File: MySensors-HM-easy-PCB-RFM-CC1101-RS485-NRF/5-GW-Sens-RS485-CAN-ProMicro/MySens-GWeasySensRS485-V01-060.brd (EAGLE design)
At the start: 33 x 50 mm, 28 parts, among them IC1 LM1117MPX-ADJ, IC2 LD117ADT50TR, IC6 LM1117MPX-ADJ, X4 1751264

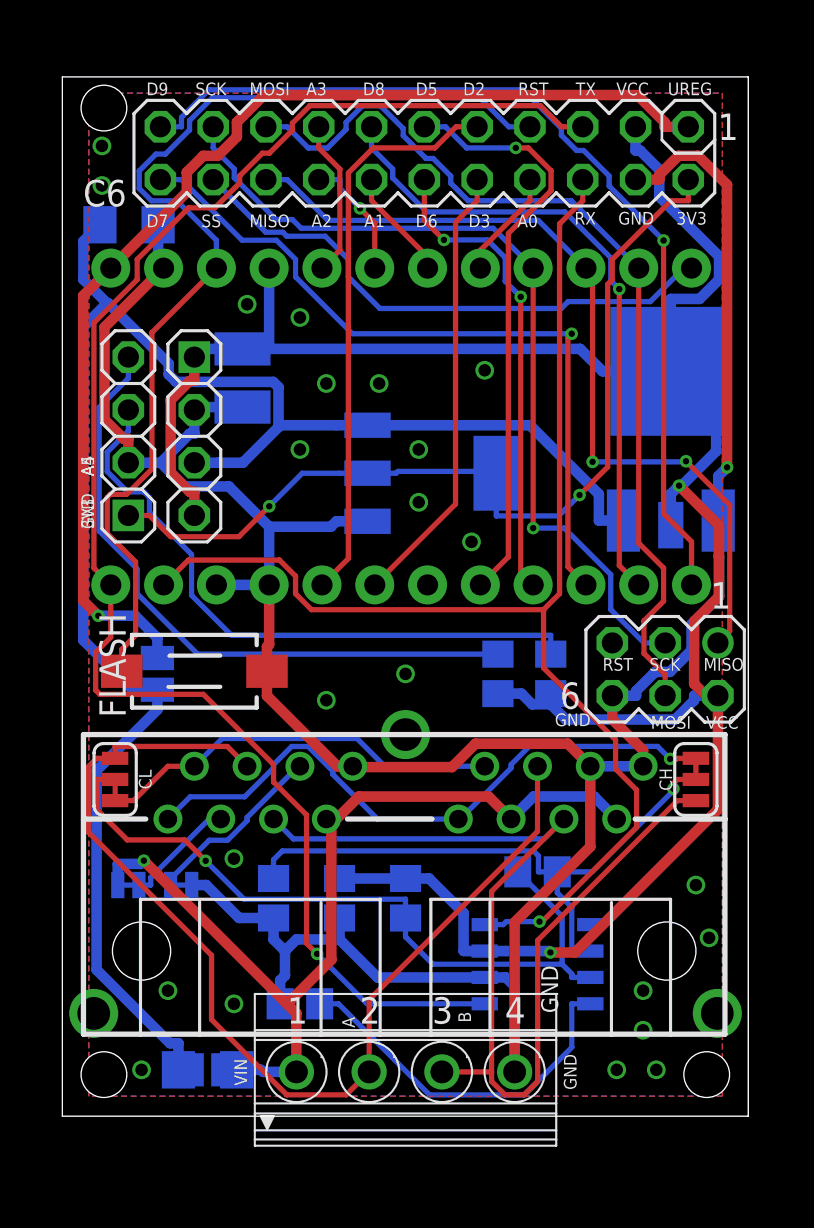
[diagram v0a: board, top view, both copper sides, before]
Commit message: CAN/RS485 Board
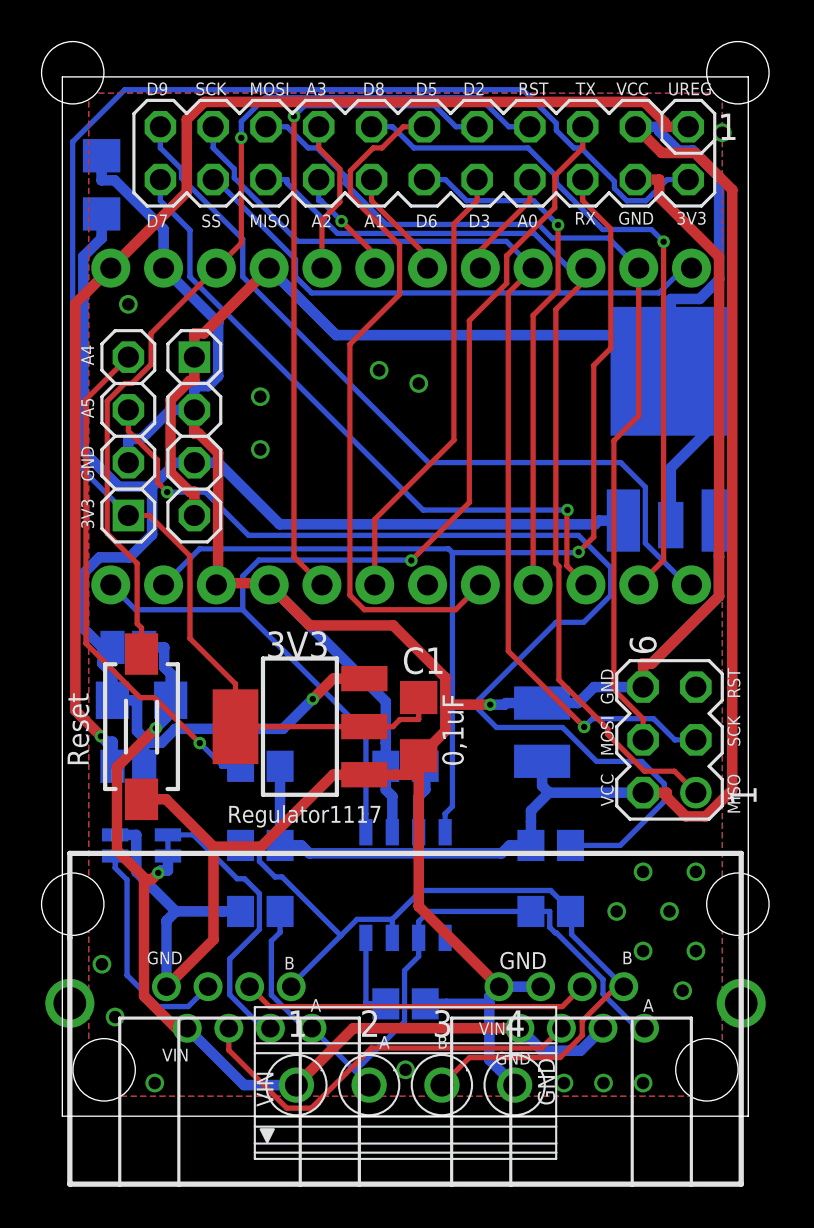
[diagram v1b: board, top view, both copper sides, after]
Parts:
- removed CH, CL: JUMPER-SMT_3_1-NC_TRACE_SILK, SparkFun-Jumpers:SMT-JUMPER_3_1-NC_TRACE_SILK
- added C1: 0.1uF, rcl:C1206
- J4: device RJ45:RJ45_2X_NARROW_SHILDPINS_NOCASE -> RJ45:RJ45_2X_S
- R3: value 680R -> 4K7
- R4: value 680R -> 4k7
- moved C4 22.3 mm to (23.1, 15.0), turned to 90 degrees
- moved RAW1 20.7 mm to (3.17, 19.1)
- moved F2 18.1 mm to (3.81, 16.5)
- moved IC1 13.7 mm to (11.4, 15.2), flipped to the top
- moved R1 12.3 mm to (9.53, 13.3), turned to 0 degrees
- moved R2 8.26 mm to (23.5, 9.53), turned to 180 degrees
- moved R3 7.43 mm to (9.53, 9.53), turned to 0 degrees
- moved U$1 7.41 mm to (16.5, 7.62), turned to 270 degrees
- moved C3 7.10 mm to (16.5, 13.3), turned to 180 degrees
- moved J4 5.71 mm to (16.5, -1.27)
- moved OPT3 5.08 mm to (16.5, 1.91), turned to 0 degrees
- moved REG_BRIDGE 4.66 mm to (3.17, 13.3), turned to 0 degrees
- moved JP3 3.70 mm to (2.54, 9.53), turned to 90 degrees
- moved FLASH 3.68 mm to (3.81, 15.2), turned to 90 degrees
- moved SV1 3.40 mm to (29.2, 14.6), turned to 90 degrees
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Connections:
- removed net H: CL.2, R3.2, R6.1, U$1.CANH
- removed net L: CH.2, R4.1, R6.2, U$1.CANL
- net 3V3: now also C1.2
- net A: now also R4.1, R6.2, U$1.CANL, X4.2; no longer CH.3
- net B: now also R3.2, R6.1, U$1.CANH, X4.3; no longer CL.3
- net CANH: no longer CL.1, X4.2
- net CANL: no longer CH.1, X4.3
- net GND: now also C1.1
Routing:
- net H: track 35.9 -> 0.00 mm, vias 1 -> 0
- net CANH: track 51.0 -> 16.8 mm
- net 3V3: track 43.8 -> 75.9 mm, vias 2 -> 0
- net CANL: track 51.2 -> 19.8 mm
- net L: track 29.3 -> 0.00 mm, vias 1 -> 0
- net GND: track 143.3 -> 168.5 mm, vias 24 -> 21
- net A5: track 30.5 -> 54.5 mm, vias 0 -> 1
- net TX1: track 76.6 -> 54.3 mm
- net B: track 19.6 -> 39.7 mm
- net VCC: track 115.9 -> 132.1 mm, vias 2 -> 0
- net RS: track 17.9 -> 4.10 mm
- net UIN: track 84.2 -> 70.6 mm, vias 0 -> 1
- net RX0: track 63.3 -> 53.5 mm
- net 1: track 5.47 -> 13.6 mm
- net D13_SCK: track 41.2 -> 49.1 mm
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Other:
- board text added: "0,1uF"
- board text added: "10K"
- board text added: "10uF"
- board text added: "1117 DPAC or SOT223"
- board text added: "22p"
- board text added: "4K7"
- board text added: "4k7"
- board text added: "C1"
- board text added: "C3"
- board text added: "C4"
- board text added: "JP-Fuse"
- board text added: "Jp1"
- board text added: "Jp3"
- board text added: "OPT3"
- board text added: "Opt.120R"
- board text added: "R1"
- board text added: "R2"
- board text added: "R3"
- board text added: "R4"
- board text added: "R6"
- board text added: "RAW1"
- board text added: "RJ45 Connector"
- board text added: "Reg"
- board text added: "RegExtern"
- board text added: "Regulator1117"
- board text added: "Reset"
- board text added: "StepDWN Vendor: OSKJ, ..."
- board text added: "opt_120R"
- board text removed: "CANH"
- board text removed: "CANL"
- board text removed: "StepDWN"
